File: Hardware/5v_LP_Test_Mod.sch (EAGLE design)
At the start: 7 parts, among them J1 CONN_3, U1 TLV61220DBV

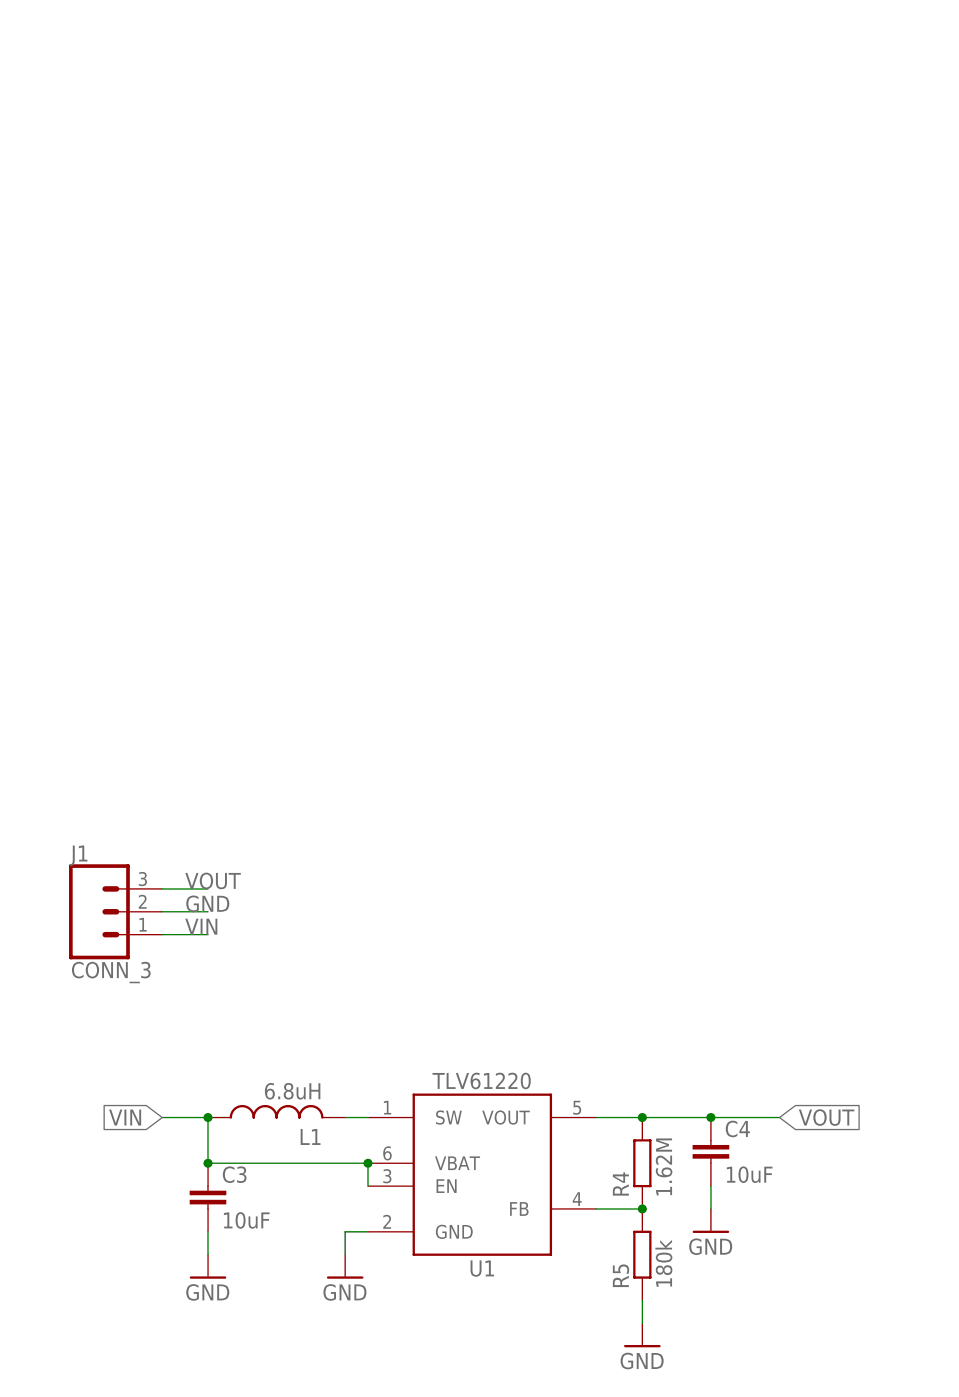
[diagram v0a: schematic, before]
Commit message: Updates to 5v test board
Added additional converter to 5v test setup, also condensed all units onto a single board and generated gerbers for compatibility with Sunstone PCB
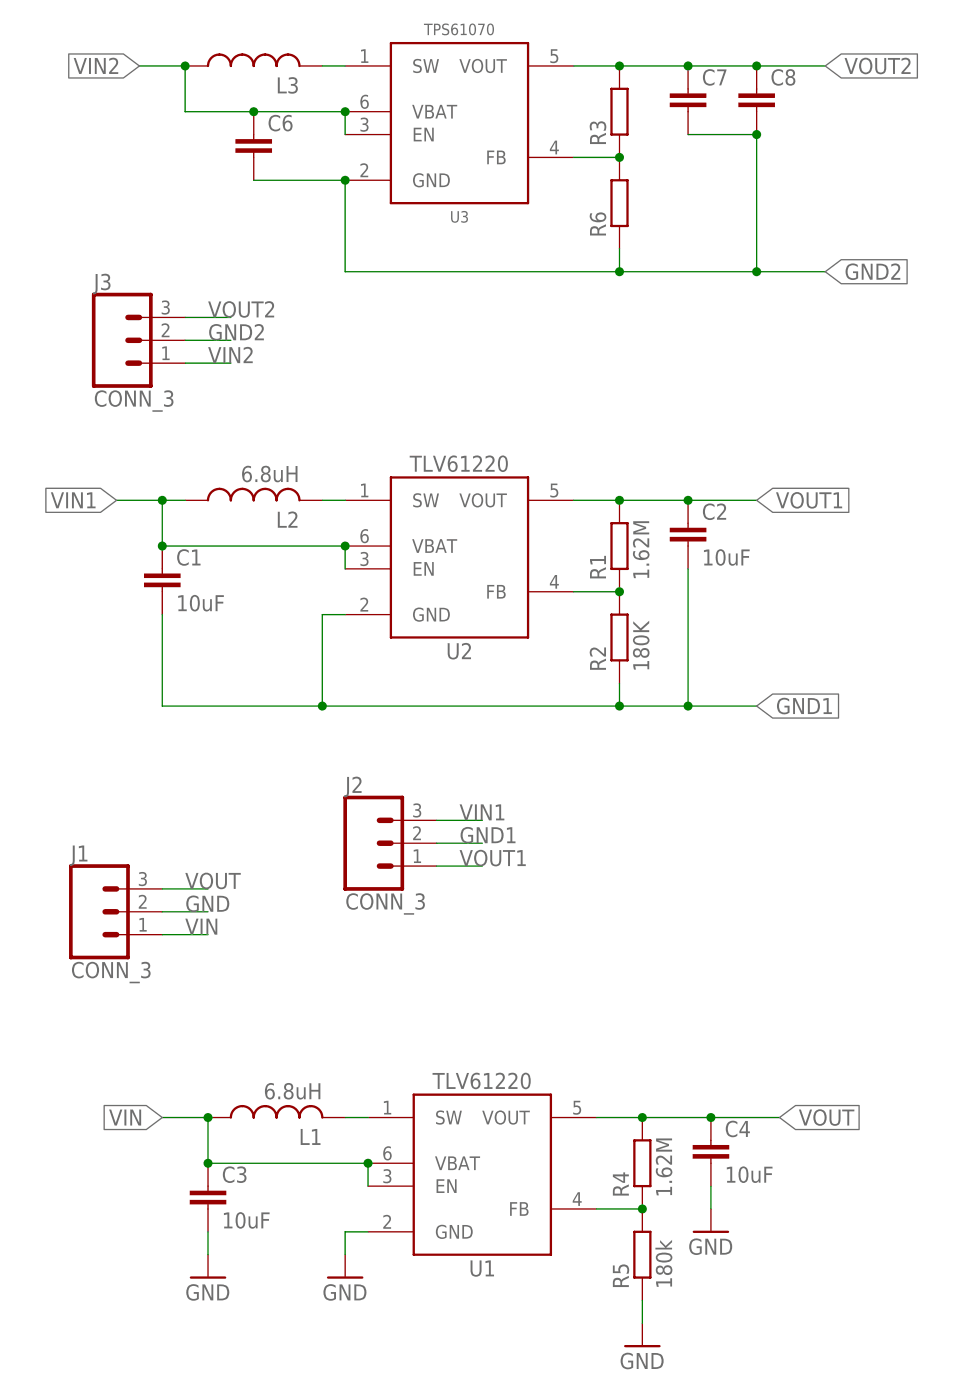
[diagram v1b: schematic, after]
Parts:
- added C1, C2: 10uF, bschulz_passives:C-EU10UFC0805
- added C6: (no value), bschulz_passives:C-EUC0805
- added C7, C8: (no value), bschulz_passives:C-EUC0603
- added J2, J3: CONN_3, bschulz:CONN_3
- added L2: 6.8uH, bschulz:INDUCTOR1008
- added L3: (no value), bschulz:INDUCTORTPC_3.8X3.8
- added R1: 1.62M, bschulz_passives:R-EU_R0603
- added R2: 180K, bschulz_passives:R-EU_R0603
- added R3, R6: (no value), bschulz_passives:R-EU_R0603
- added U2: TLV61220DBV, bschulz:TLV61220DBV
- added U3: TPS61070DDC, bschulz:TPS61070DDC
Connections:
- new net GND1: C1.2, C2.2, J2.2, R2.1, U2.GND
- new net GND2: C6.2, C7.2, C8.2, J3.2, R6.1, U3.GND
- new net N$1: R1.1, R2.2, U2.FB
- new net N$2: L3.2, U3.SW
- new net N$5: L2.2, U2.SW
- new net N$6: R3.1, R6.2, U3.FB
- new net VIN1: C1.1, J2.3, L2.1, U2.EN, U2.VBAT
- new net VIN2: C6.1, J3.1, L3.1, U3.EN, U3.VBAT
- new net VOUT1: C2.1, J2.1, R1.2, U2.VOUT
- new net VOUT2: C7.1, C8.1, J3.3, R3.2, U3.VOUT
